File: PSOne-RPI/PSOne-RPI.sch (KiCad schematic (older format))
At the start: 1 part

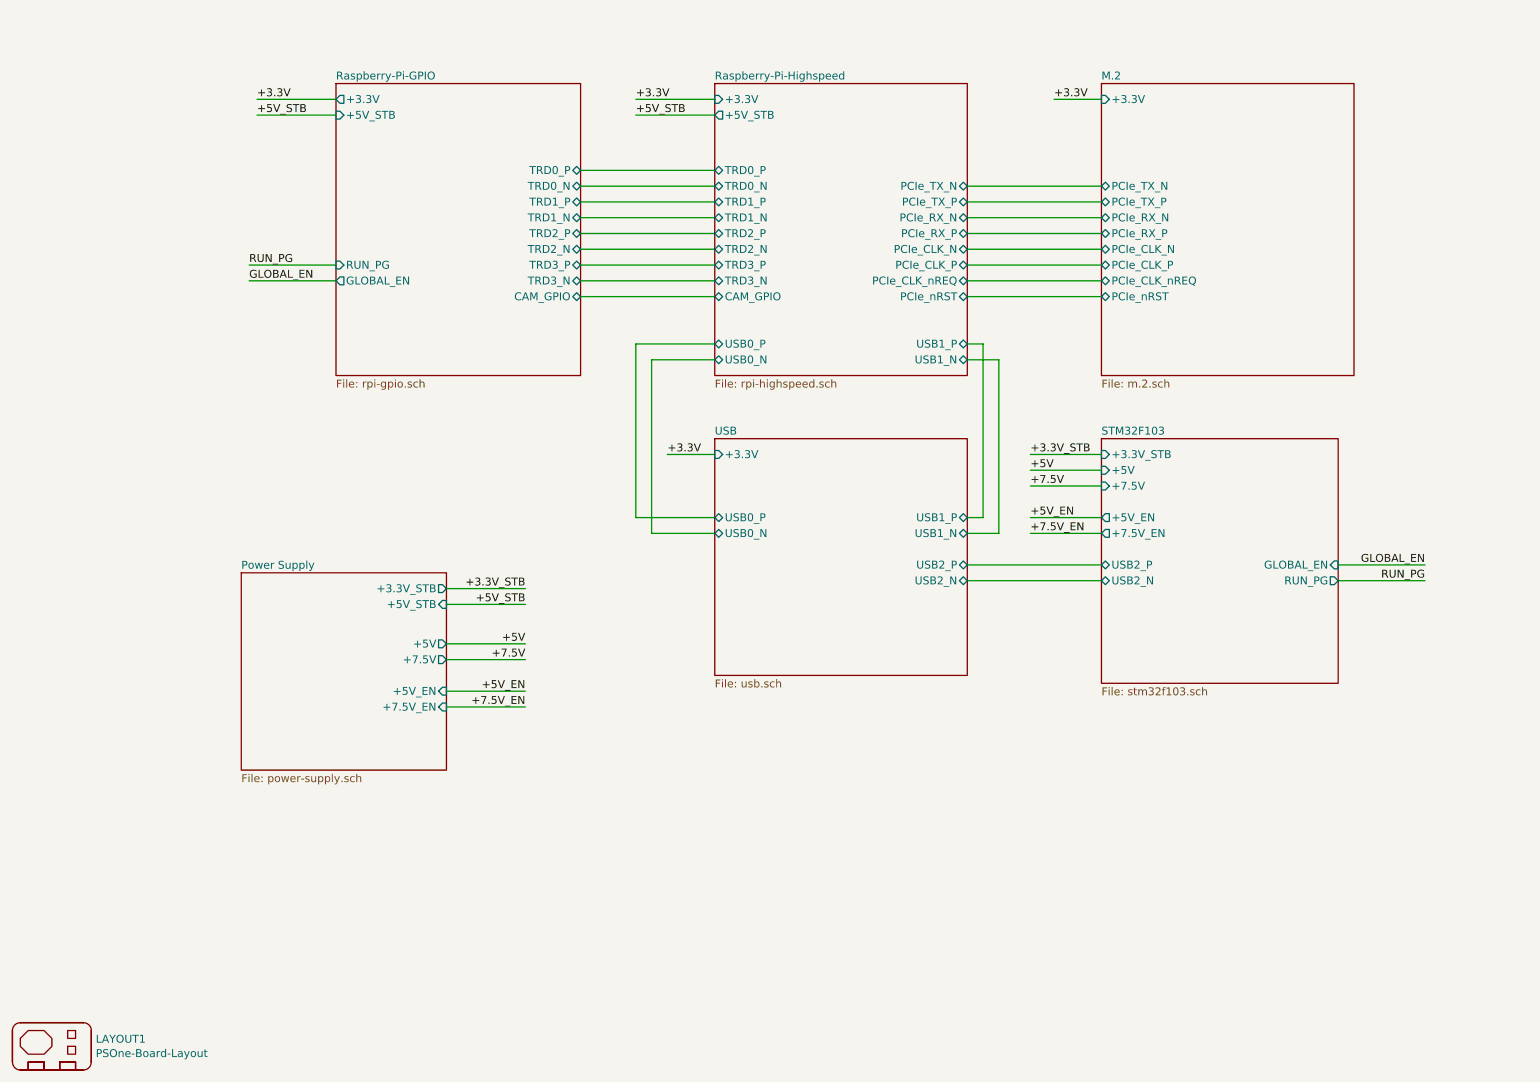
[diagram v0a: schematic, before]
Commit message: Cleaned schematic and moved CD interface to extra sheet
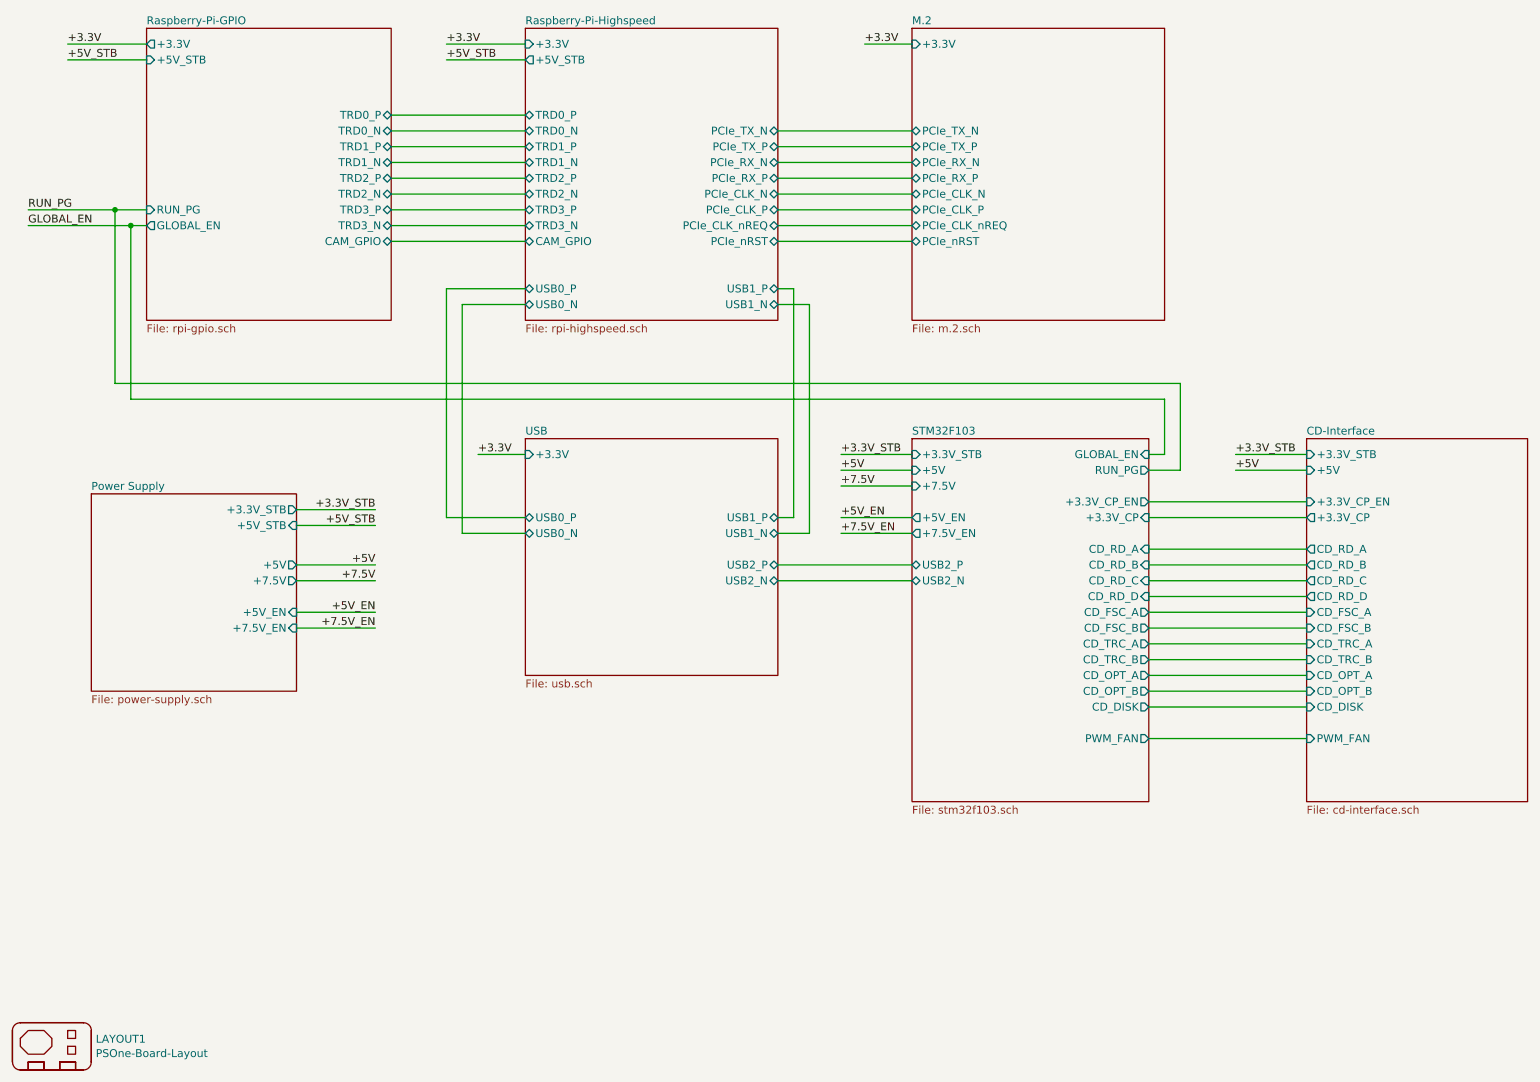
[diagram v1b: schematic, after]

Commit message: Finished CD drive interface circuit
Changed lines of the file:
@@
 F22 "CD_OPT_B" O R 7900 5200 50
 F23 "CD_DISK" O R 7900 5300 50
-F24 "PWM_FAN" O R 7900 5500 50
+F24 "PWM_FAN" O R 7900 5800 50
+F25 "CD_MD" O R 7900 5400 50
+F26 "CD_STOP" I R 7900 5500 50
+F27 "CD_LD" O R 7900 5600 50
 $EndSheet
 Text Label 6100 1100 0    50   ~ 0
@@
 F15 "CD_OPT_B" I L 8900 5200 50
 F16 "CD_DISK" I L 8900 5300 50
-F17 "PWM_FAN" I L 8900 5500 50
+F17 "PWM_FAN" I L 8900 5800 50
+F18 "CD_MD" I L 8900 5400 50
+F19 "CD_STOP" O L 8900 5500 50
+F20 "CD_LD" I L 8900 5600 50
 $EndSheet
 Wire Wire Line
@@
 	7900 5300 8900 5300
 Wire Wire Line
-	8900 5500 7900 5500
+	8900 5600 7900 5600
+Wire Wire Line
+	7900 5500 8900 5500
+Wire Wire Line
+	8900 5400 7900 5400
+Wire Wire Line
+	7900 5800 8900 5800
 $EndSCHEMATC

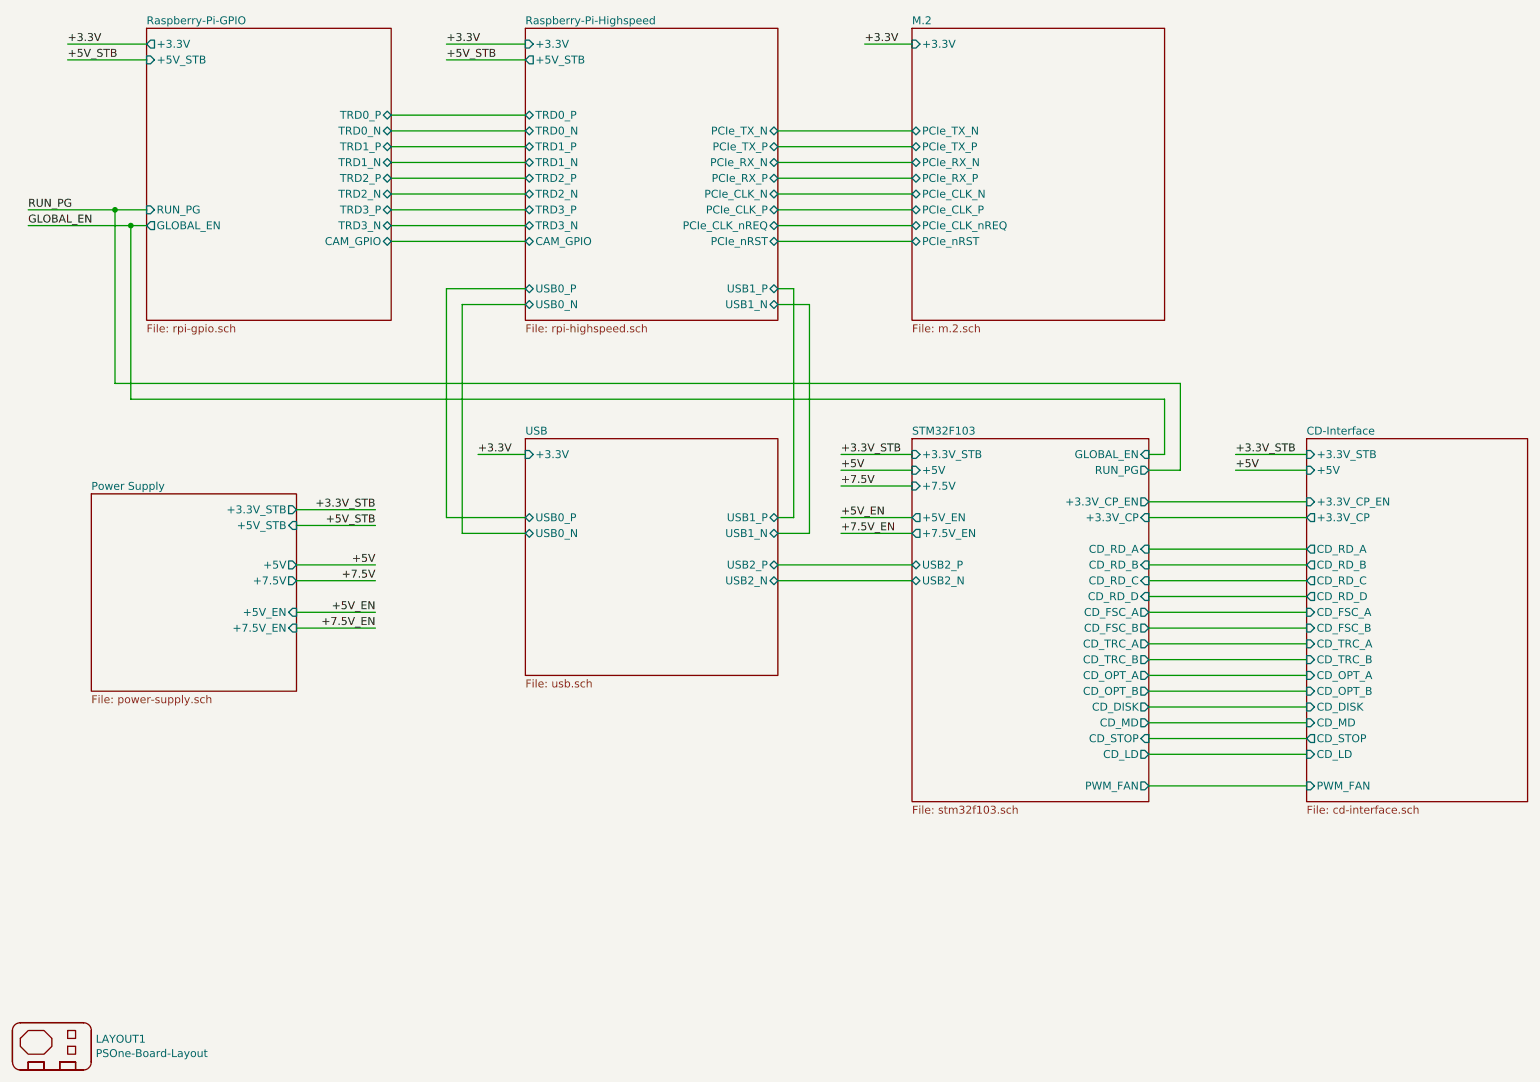
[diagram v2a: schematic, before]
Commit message: Added possibility to use the STM32 as RTC
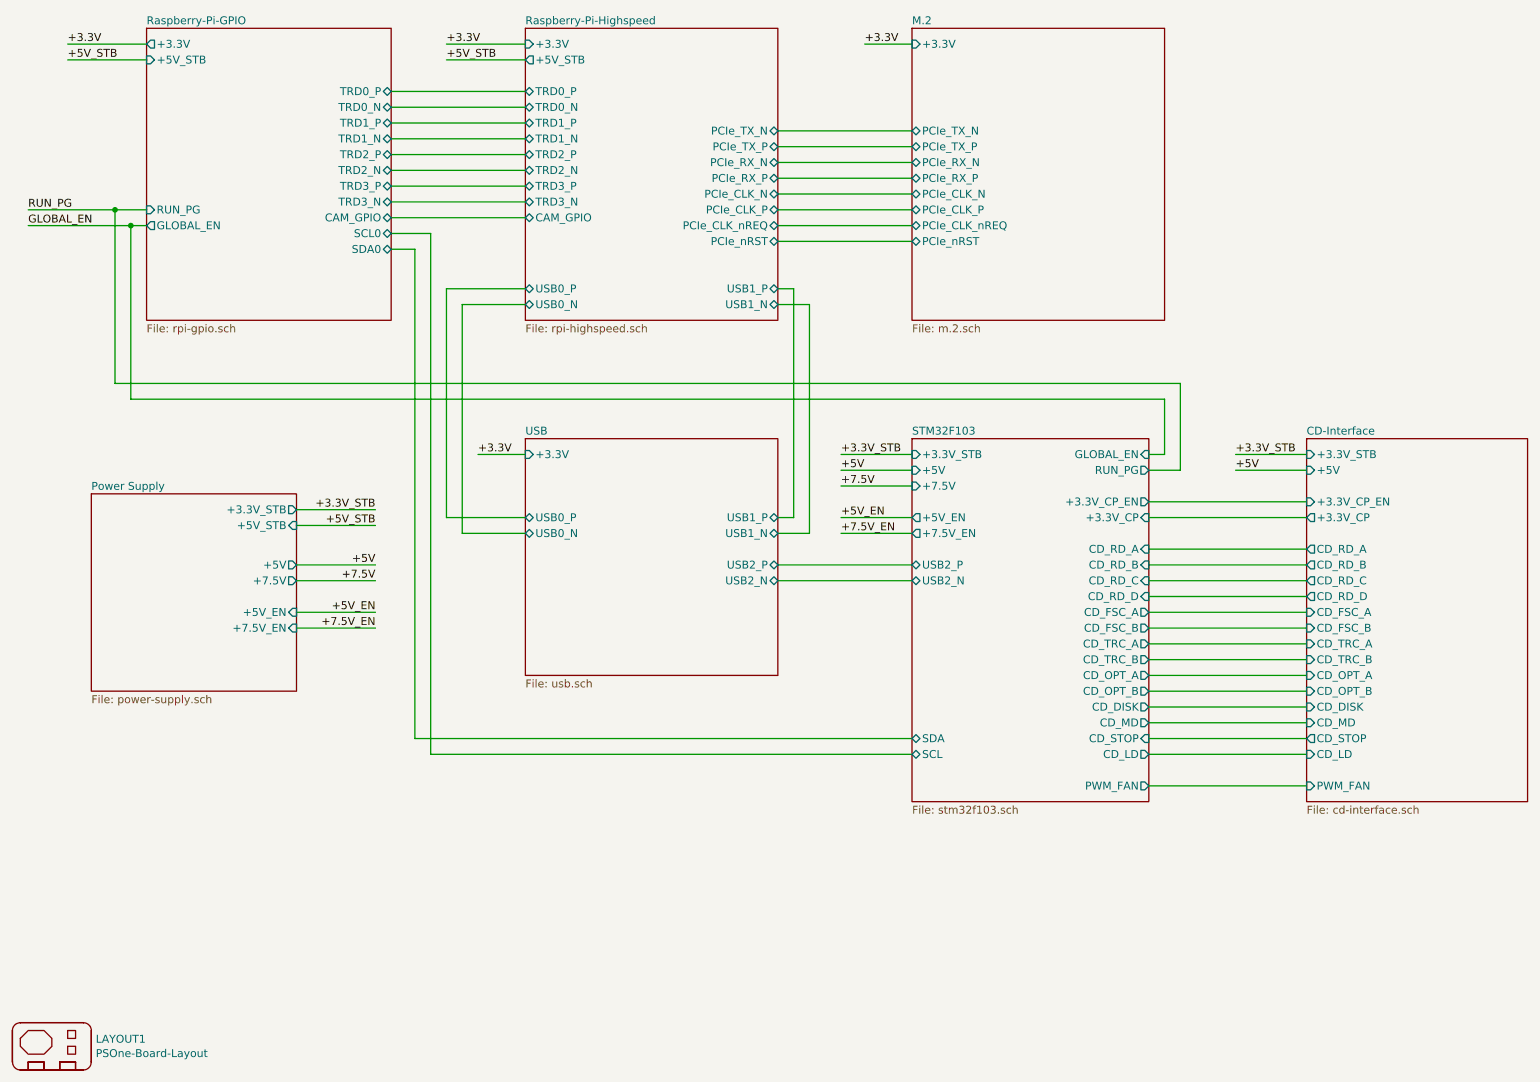
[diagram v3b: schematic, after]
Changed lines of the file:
@@
 F0 "Raspberry-Pi-GPIO" 50
 F1 "rpi-gpio.sch" 50
-F2 "TRD1_P" B R 3100 1750 50
-F3 "TRD1_N" B R 3100 1850 50
-F4 "TRD0_P" B R 3100 1550 50
-F5 "TRD0_N" B R 3100 1650 50
-F6 "TRD3_P" B R 3100 2150 50
-F7 "TRD3_N" B R 3100 2250 50
-F8 "TRD2_P" B R 3100 1950 50
-F9 "TRD2_N" B R 3100 2050 50
+F2 "TRD1_P" B R 3100 1600 50
+F3 "TRD1_N" B R 3100 1700 50
+F4 "TRD0_P" B R 3100 1400 50
+F5 "TRD0_N" B R 3100 1500 50
+F6 "TRD3_P" B R 3100 2000 50
+F7 "TRD3_N" B R 3100 2100 50
+F8 "TRD2_P" B R 3100 1800 50
+F9 "TRD2_N" B R 3100 1900 50
 F10 "+5V_STB" I L 1550 1200 50
 F11 "RUN_PG" I L 1550 2150 50
 F12 "GLOBAL_EN" O L 1550 2250 50
-F13 "CAM_GPIO" B R 3100 2350 50
+F13 "CAM_GPIO" B R 3100 2200 50
 F14 "+3.3V" O L 1550 1100 50
+F15 "SCL0" B R 3100 2300 50
+F16 "SDA0" B R 3100 2400 50
 $EndSheet
 $Sheet
@@
 F0 "Raspberry-Pi-Highspeed" 50
 F1 "rpi-highspeed.sch" 50
-F2 "TRD1_P" B L 3950 1750 50
-F3 "TRD1_N" B L 3950 1850 50
-F4 "TRD0_P" B L 3950 1550 50
-F5 "TRD0_N" B L 3950 1650 50
-F6 "TRD3_P" B L 3950 2150 50
-F7 "TRD3_N" B L 3950 2250 50
-F8 "TRD2_P" B L 3950 1950 50
-F9 "TRD2_N" B L 3950 2050 50
+F2 "TRD1_P" B L 3950 1600 50
+F3 "TRD1_N" B L 3950 1700 50
+F4 "TRD0_P" B L 3950 1400 50
+F5 "TRD0_N" B L 3950 1500 50
+F6 "TRD3_P" B L 3950 2000 50
+F7 "TRD3_N" B L 3950 2100 50
+F8 "TRD2_P" B L 3950 1800 50
+F9 "TRD2_N" B L 3950 1900 50
 F10 "PCIe_TX_N" B R 5550 1650 50
 F11 "PCIe_TX_P" B R 5550 1750 50
@@
 F22 "+3.3V" I L 3950 1100 50
 F23 "+5V_STB" O L 3950 1200 50
-F24 "CAM_GPIO" B L 3950 2350 50
+F24 "CAM_GPIO" B L 3950 2200 50
 $EndSheet
 $Comp
@@
 $EndSheet
 Wire Wire Line
-	3100 1550 3950 1550
-Wire Wire Line
-	3950 1650 3100 1650
-Wire Wire Line
-	3100 1750 3950 1750
-Wire Wire Line
-	3950 1850 3100 1850
-Wire Wire Line
-	3100 1950 3950 1950
-Wire Wire Line
-	3950 2050 3100 2050
-Wire Wire Line
-	3100 2150 3950 2150
-Wire Wire Line
-	3950 2250 3100 2250
+	3100 1400 3950 1400
+Wire Wire Line
+	3950 1500 3100 1500
+Wire Wire Line
+	3100 1600 3950 1600
+Wire Wire Line
+	3950 1700 3100 1700
+Wire Wire Line
+	3100 1800 3950 1800
+Wire Wire Line
+	3950 1900 3100 1900
+Wire Wire Line
+	3100 2000 3950 2000
+Wire Wire Line
+	3950 2100 3100 2100
 Wire Wire Line
 	5550 1650 6400 1650
@@
 F26 "CD_STOP" I R 7900 5500 50
 F27 "CD_LD" O R 7900 5600 50
+F28 "SDA" B L 6400 5500 50
+F29 "SCL" B L 6400 5600 50
 $EndSheet
 Text Label 6100 1100 0    50   ~ 0
@@
 RUN_PG
 Wire Wire Line
-	3100 2350 3950 2350
+	3100 2200 3950 2200
 $Sheet
 S 8900 3600 1400 2300
@@
 Wire Wire Line
 	7900 5800 8900 5800
+Wire Wire Line
+	3100 2300 3350 2300
+Wire Wire Line
+	3350 2300 3350 5600
+Wire Wire Line
+	3350 5600 6400 5600
+Wire Wire Line
+	3100 2400 3250 2400
+Wire Wire Line
+	3250 2400 3250 5500
+Wire Wire Line
+	3250 5500 6400 5500
 $EndSCHEMATC
